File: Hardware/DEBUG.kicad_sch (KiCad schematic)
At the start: 1 part, among them CN1 HX JN1.27-2X5 TP H4.9

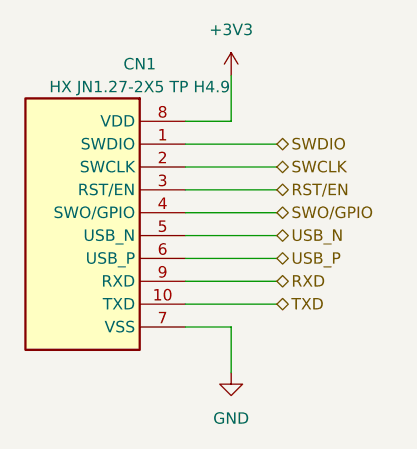
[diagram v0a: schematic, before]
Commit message: remove unused sheets
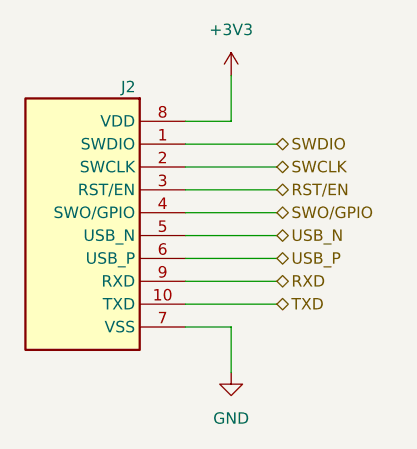
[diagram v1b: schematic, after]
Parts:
- removed CN1: HX JN1.27-2X5 TP H4.9, EasyEDA:IDC-TH_10P-P1.27-V-M-R2-C5-S1.27, symbol EasyEDA:HXJN1.27-2X5TPH4.9
- added J2: Connector, USB-TYPE-C-16P, EasyEDA:IDC-SMD_10P-P1.27-3220-10-0300-00, symbol PCM_JLCPCB-Extended:Connector, AT Debug P1.27
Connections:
- net +3V3: now also J2.8 (VDD)
- net GND: now also J2.7 (VSS)
- net RST/EN: now also J2.3 (RST/EN)
- net RXD: now also J2.9 (RXD)
- net SWCLK: now also J2.2 (SWCLK)
- net SWDIO: now also J2.1 (SWDIO)
- net SWO/GPIO: now also J2.4 (SWO/GPIO)
- net TXD: now also J2.10 (TXD)
- net USB_N: now also J2.5 (USB_N)
- net USB_P: now also J2.6 (USB_P)
